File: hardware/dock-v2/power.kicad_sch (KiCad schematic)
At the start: 27 parts, among them J101 TYPE-C-31-M-12, U101 TPD4E1U06DBVR, U102 CH224A, U103 TPS54331DR, U104 AMS1117-3.3

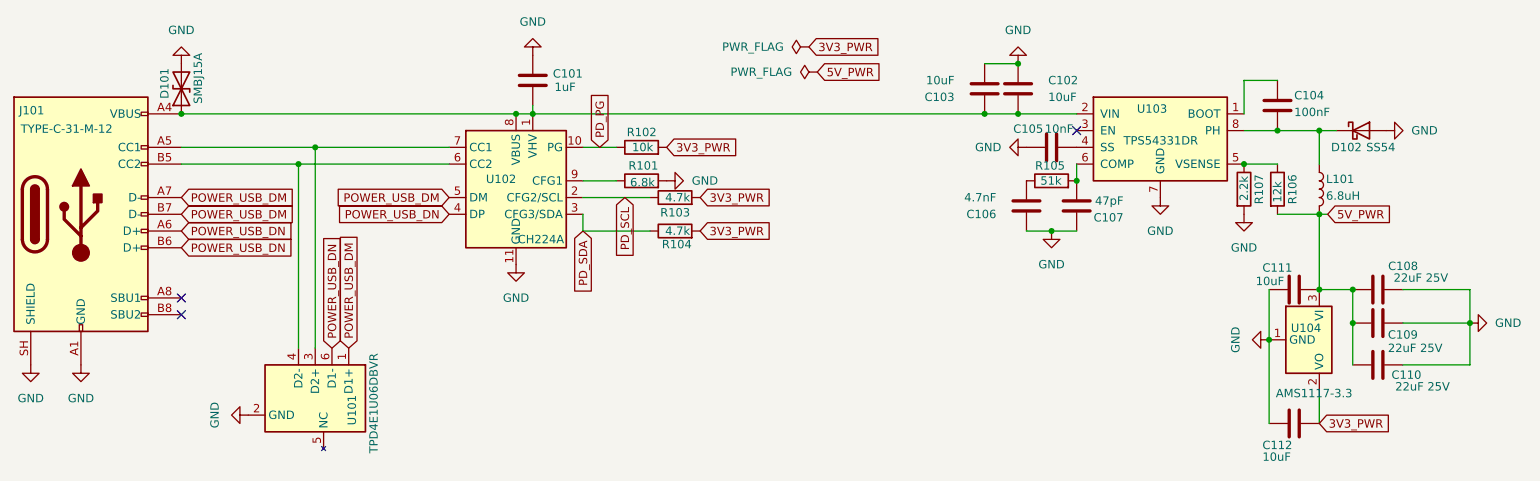
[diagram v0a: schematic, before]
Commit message: Dock v2 schematic: pogo sheet wired, fixes from review (user's work, snapshot)
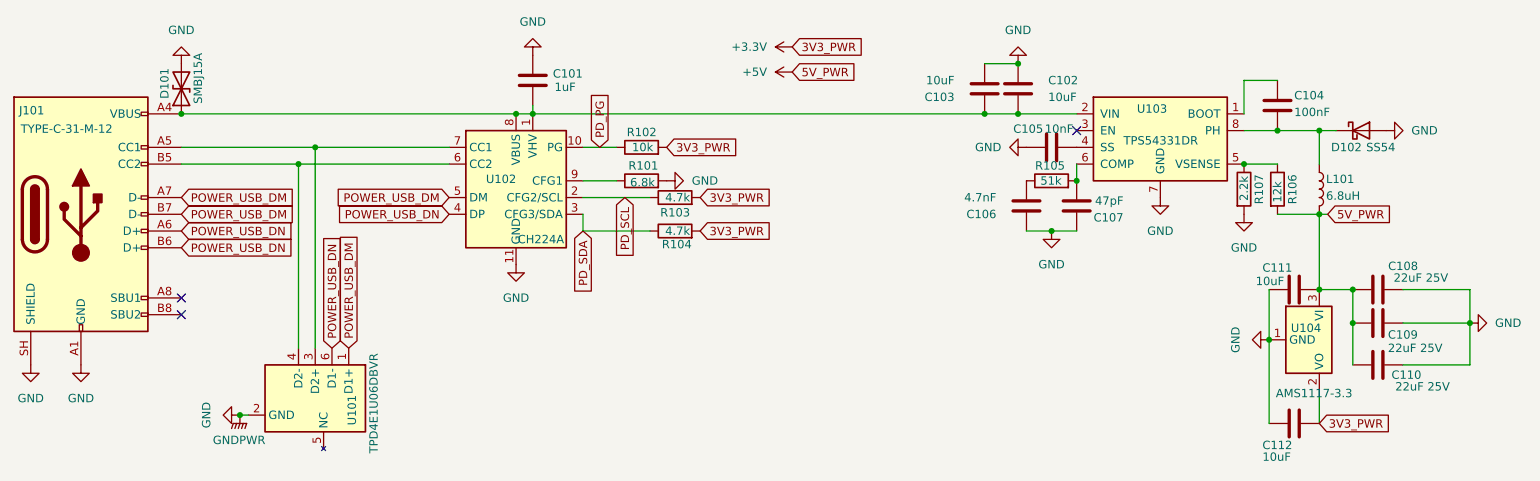
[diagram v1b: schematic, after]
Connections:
- net 3V3_PWR renamed +3.3V
- net 5V_PWR renamed +5V
